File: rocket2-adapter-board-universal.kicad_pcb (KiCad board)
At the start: 2 copper layers, 45 x 55 mm, 15 parts, among them J2 Conn_01x04_Socket, J3 Conn_01x02_Socket, J4 Conn_01x04_Socket, J5 DSUB_15pin/VGA Veritical Fema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

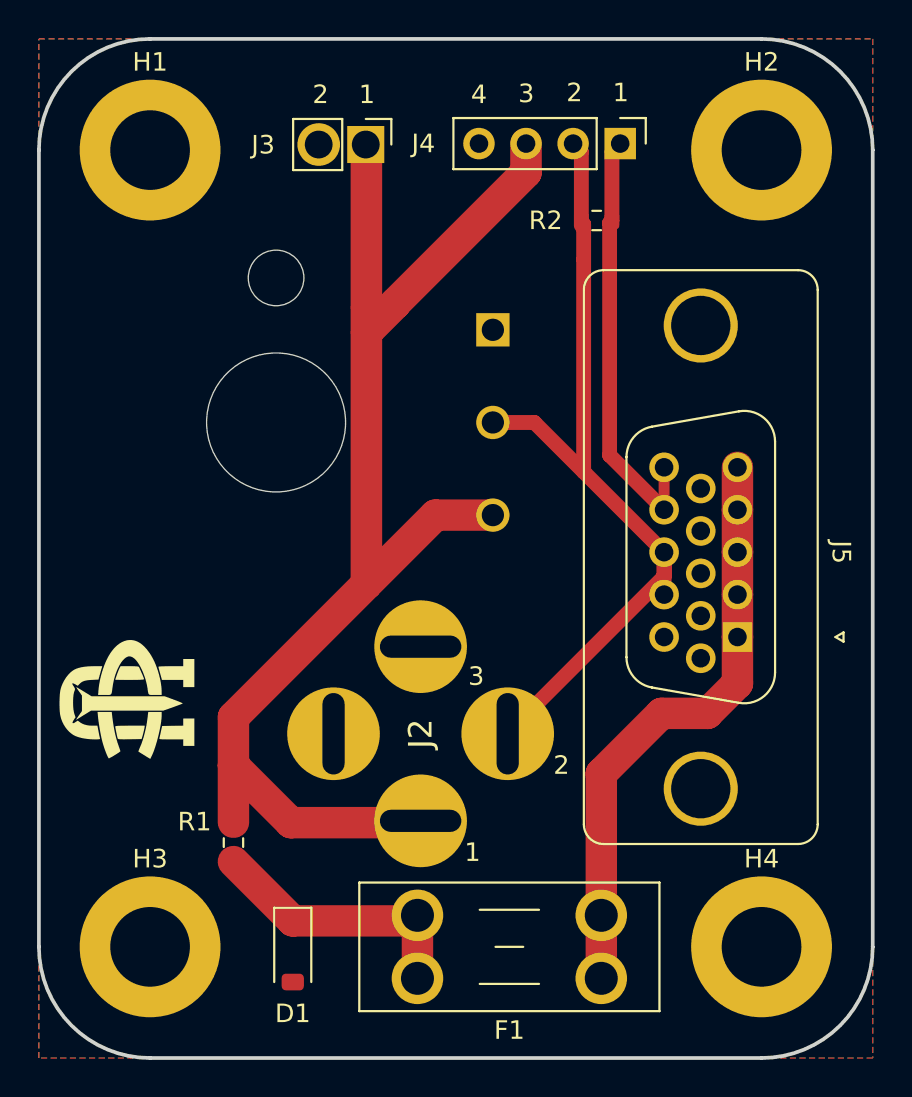
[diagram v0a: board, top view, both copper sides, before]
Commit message: Layout Update 6: Updated PT footprint, Silkscreen labels, M3s
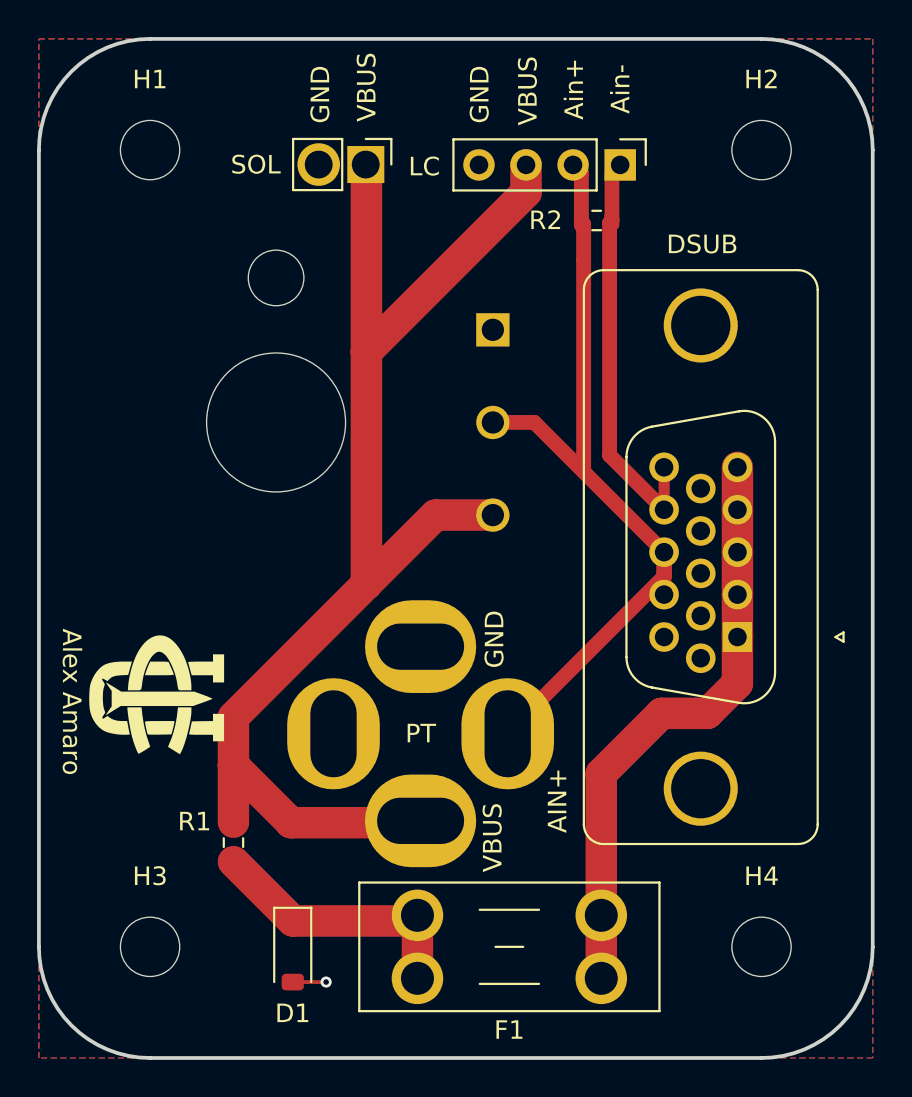
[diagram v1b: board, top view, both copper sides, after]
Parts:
- H1, H2, H3, H4: footprint MountingHole:MountingHole_4.3mm_M4_ISO7380_Pad -> MountingHole:MountingHole_3.2mm_M3_ISO7380
- moved REF** 1.62 mm to (126.5, 95.6)
- moved J4 1.15 mm to (151.4, 66.8)
- moved J3 1.08 mm to (136.4, 66.8)
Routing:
- net GND: track 0.00 -> 1.80 mm, vias 0 -> 1
- net VBUS: track 73.0 -> 71.8 mm
- net AIN-: track 24.2 -> 23.1 mm
- net AIN+: track 46.7 -> 45.5 mm
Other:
- board text added: "AIN+"
- board text added: "Ain+"
- board text added: "Ain-"
- board text added: "Alex Amaro"
- board text added: "DSUB"
- board text added: "GND"
- board text added: "LC"
- board text added: "POT"
- board text added: "PT"
- board text added: "SOL"
- board text added: "VBUS"
- board text removed: "1"
- board text removed: "2"
- board text removed: "3"
- board text removed: "4"

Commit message: Ready for purchasing
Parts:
- H1: footprint MountingHole:MountingHole_3.2mm_M3_ISO7380 -> MountingHole:MountingHole_3.2mm_M3_DIN965_Pad
- H2, H3, H4: footprint MountingHole:MountingHole_3.2mm_M3_ISO7380 -> MountingHole:MountingHole_3.2mm_M3_ISO7380_Pad
- moved REF** 6.59 mm to (125.5, 102.1), turned to 90 degrees
- moved R1 3.50 mm to (134.0, 103.2)
- moved G*** 2.43 mm to (128.0, 96.2)
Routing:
- net VBUS: track 71.8 -> 60.0 mm
- net Net-(D1-K): track 14.8 -> 14.0 mm
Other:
- board text added: "By: Alex Amaro April 2026"
- board text added: "Universal Sensor Adapter Board"
- board text removed: "Alex Amaro"

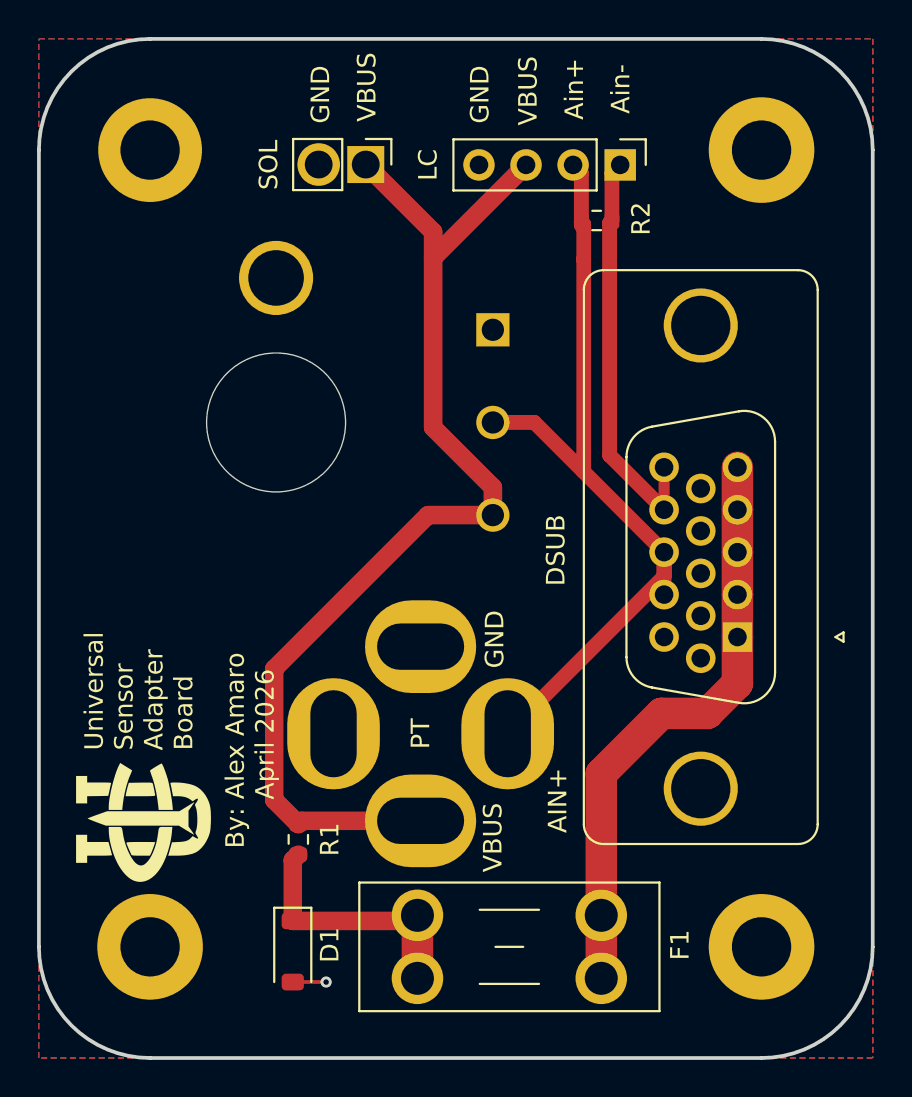
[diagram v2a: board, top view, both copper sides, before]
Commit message: Repositioned things so it would fit better
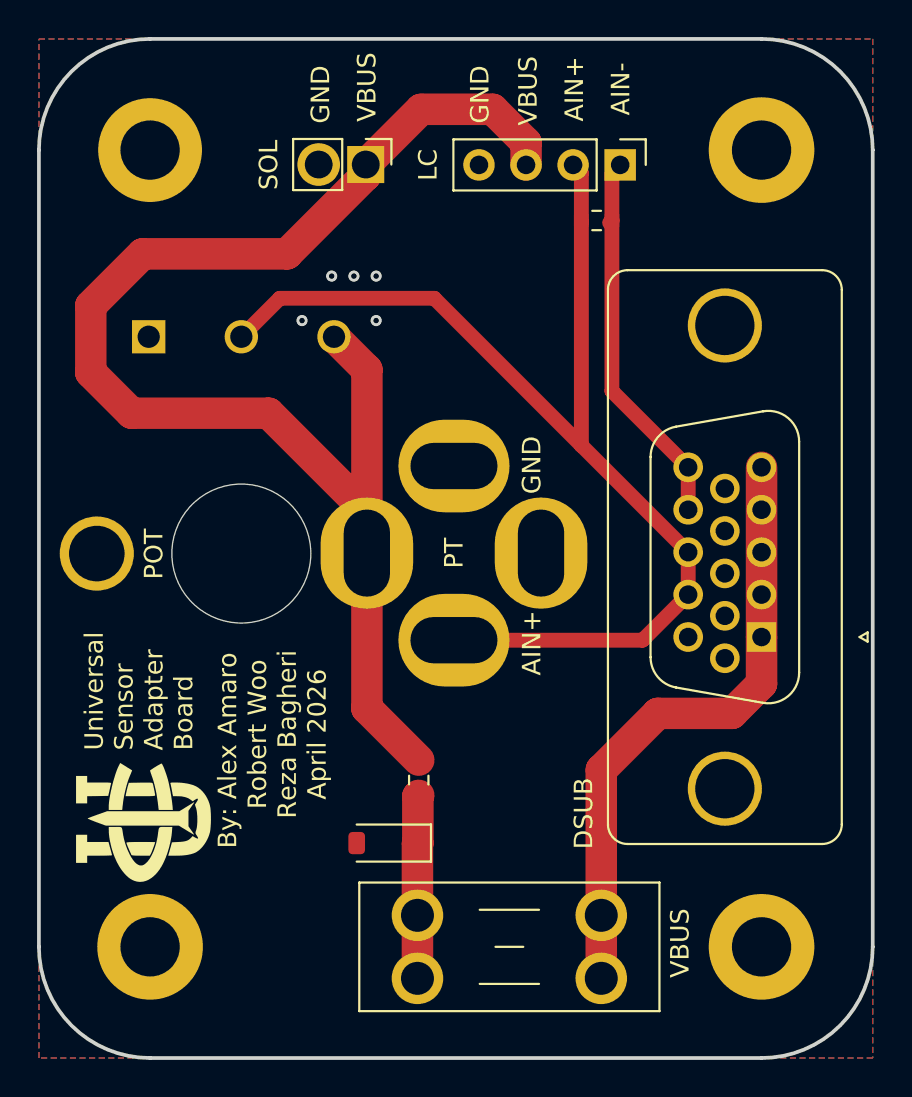
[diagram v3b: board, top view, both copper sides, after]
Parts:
- added G***: LOGO, LOGO, B.Cu at (156.4, 97.2)
- moved VR1 18.6 mm to (125.9, 76.1), turned to 0 degrees
- moved J2 9.91 mm to (142.4, 87.8), turned to 0 degrees
- moved D1 7.76 mm to (138.8, 103.4), turned to 180 degrees
- moved R1 7.24 mm to (140.5, 100.0)
- moved G*** 2.20 mm to (126.8, 98.0)
- moved J5 1.30 mm to (167.5, 87.7)
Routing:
- net VBUS: track 60.0 -> 78.8 mm
- net AIN+: track 45.5 -> 62.2 mm
- net Net-(D1-K): track 14.0 -> 9.90 mm
- net AIN-: track 23.1 -> 20.7 mm
- net GND: track 1.80 -> 0.00 mm, vias 1 -> 5
- net VIN: track 32.1 -> 33.5 mm
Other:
- board text added: "AIN-"
- board text added: "By: Alex Amaro Robert Woo Reza Bagheri April 2026"
- board text removed: "Ain+"
- board text removed: "Ain-"
- board text removed: "By: Alex Amaro April 2026"

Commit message: Updated for order
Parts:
- added G***: LOGO, LOGO, B.Cu at (155.2, 88.0)
- added G***: LOGO, LOGO, B.Cu at (125.8, 73.2)
- moved G*** 29.8 mm to (142.6, 70.8)
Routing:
- net GND: vias 5 -> 6
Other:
- board text added: "Break this, prop."
- board text added: "千空"
